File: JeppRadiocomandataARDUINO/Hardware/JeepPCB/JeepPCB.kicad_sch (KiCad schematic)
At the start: 10 parts

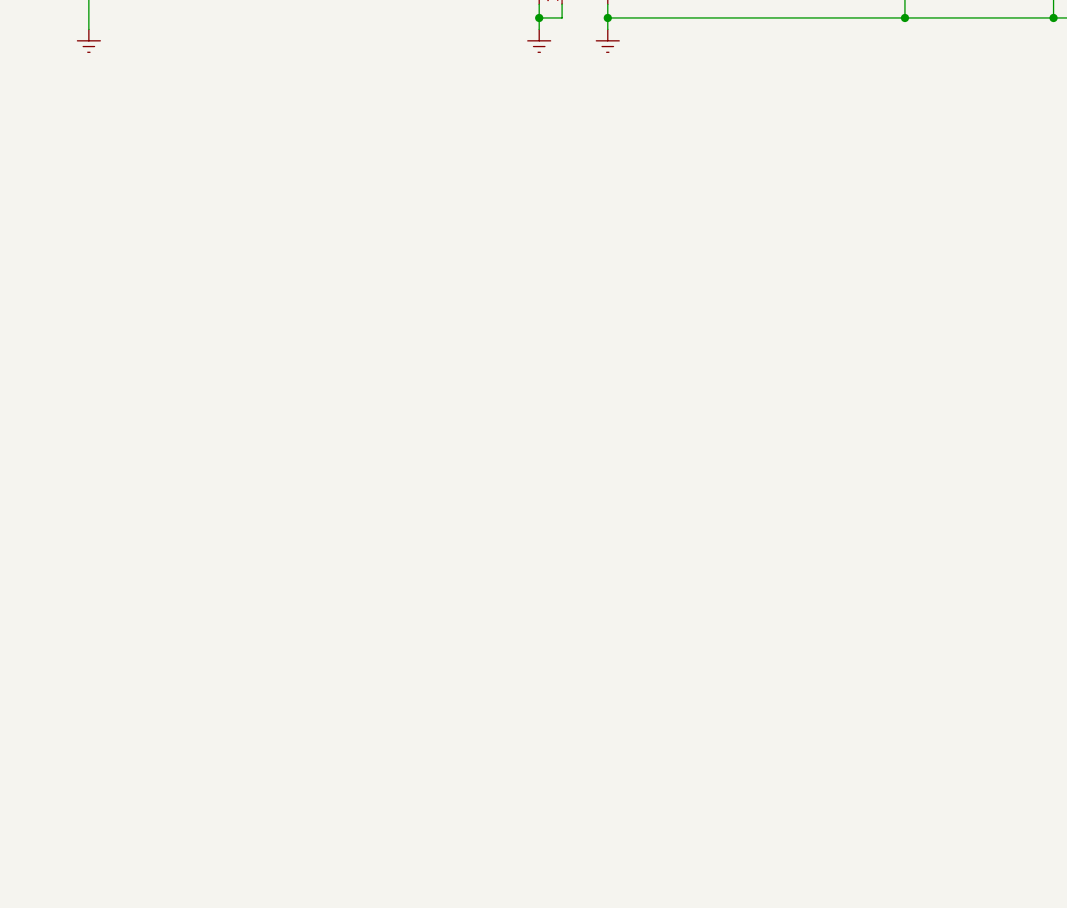
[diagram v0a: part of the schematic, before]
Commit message: Aggiunta della CPU ATmega328P
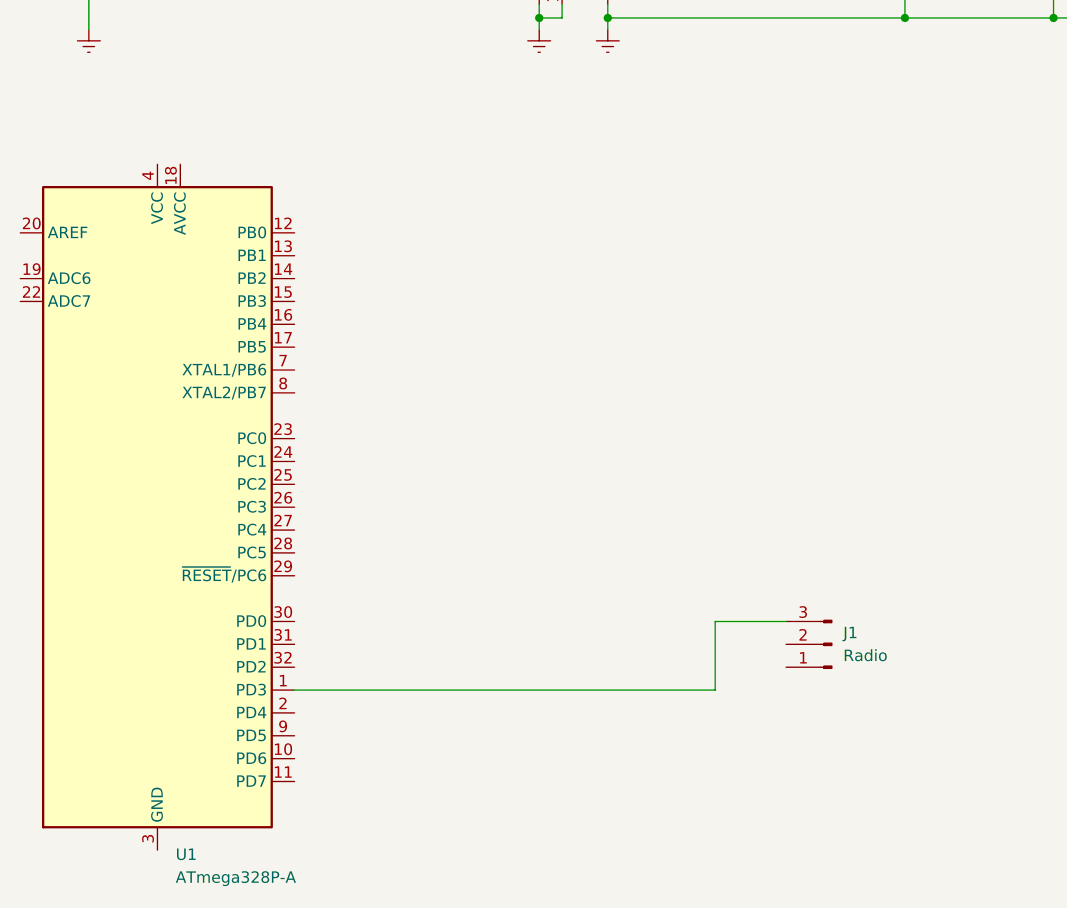
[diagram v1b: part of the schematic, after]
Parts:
- added J1: Radio, Connector_PinHeader_1.00mm:PinHeader_1x03_P1.00mm_Vertical, symbol Connector:Conn_01x03_Male
- added U1: ATmega328P-A, Package_QFP:TQFP-32_7x7mm_P0.8mm, symbol MCU_Microchip_ATmega:ATmega328P-A
- D1, D2, D3, D4, D5, D6, D7, D8: footprint Diode_THT:D_DO-41_SOD81_P10.16mm_Horizontal -> Diode_SMD:D_0402_1005Metric_Pad0.77x0.64mm_HandSolder
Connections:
- new net: J1.3 (Pin_3), U1.1 (PD3)
- new net: U1.21 (GND), U1.3 (GND), U1.5 (GND)
- new net: U1.4 (VCC), U1.6 (VCC)
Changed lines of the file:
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@@
   (junction (at 132.588 50.8) (diameter 0) (color 0 0 0 0)
   )
+  (junction (at 147.574 82.296) (diameter 0) (color 0 0 0 0)
+  )
+  (junction (at 147.574 53.848) (diameter 0) (color 0 0 0 0)
+  )
+  (junction (at 75.438 82.296) (diameter 0) (color 0 0 0 0)
+  )
+  (junction (at 116.078 57.912) (diameter 0) (color 0 0 0 0)
+  )
   (junction (at 83.058 82.296) (diameter 0) (color 0 0 0 0)
   )
-  (junction (at 147.574 82.296) (diameter 0) (color 0 0 0 0)
-  )
-  (junction (at 147.574 53.848) (diameter 0) (color 0 0 0 0)
-  )
-  (junction (at 75.438 82.296) (diameter 0) (color 0 0 0 0)
-  )
-  (junction (at 116.078 57.912) (diameter 0) (color 0 0 0 0)
-  )
   (junction (at 132.588 60.452) (diameter 0) (color 0 0 0 0)
   )
@@
     (stroke (width 0) (type default) (color 0 0 0 0))
   )
+  (wire (pts (xy 83.058 80.772) (xy 83.058 82.296))
+    (stroke (width 0) (type default) (color 0 0 0 0))
+  )
   (wire (pts (xy 98.298 65.532) (xy 147.574 65.532))
     (stroke (width 0) (type default) (color 0 0 0 0))
@@
     (stroke (width 0) (type default) (color 0 0 0 0))
   )
-  (wire (pts (xy 83.058 80.772) (xy 83.058 82.296))
+  (wire (pts (xy 48.26 156.972) (xy 94.996 156.972))
     (stroke (width 0) (type default) (color 0 0 0 0))
   )
@@
     (stroke (width 0) (type default) (color 0 0 0 0))
   )
+  (wire (pts (xy 94.996 149.352) (xy 102.87 149.352))
+    (stroke (width 0) (type default) (color 0 0 0 0))
+  )
   (wire (pts (xy 147.574 80.01) (xy 147.574 82.296))
     (stroke (width 0) (type default) (color 0 0 0 0))
@@
   )
   (wire (pts (xy 116.078 82.296) (xy 132.588 82.296))
+    (stroke (width 0) (type default) (color 0 0 0 0))
+  )
+  (wire (pts (xy 94.996 149.352) (xy 94.996 156.972))
     (stroke (width 0) (type default) (color 0 0 0 0))
   )
@@
       (effects (font (size 1.27 1.27)) (justify left))
     )
-    (property "Footprint" "Diode_THT:D_DO-41_SOD81_P10.16mm_Horizontal" (id 2) (at 111.633 38.608 0)
+    (property "Footprint" "Diode_SMD:D_0402_1005Metric_Pad0.77x0.64mm_HandSolder" (id 2) (at 111.633 38.608 0)
       (effects (font (size 1.27 1.27)) hide)
     )
@@
       (effects (font (size 1.27 1.27)) (justify left))
     )
-    (property "Footprint" "Diode_THT:D_DO-41_SOD81_P10.16mm_Horizontal" (id 2) (at 143.129 38.608 0)
+    (property "Footprint" "Diode_SMD:D_0402_1005Metric_Pad0.77x0.64mm_HandSolder" (id 2) (at 143.129 38.608 0)
       (effects (font (size 1.27 1.27)) hide)
     )
@@
       (effects (font (size 1.27 1.27)) (justify left))
     )
-    (property "Footprint" "Diode_THT:D_DO-41_SOD81_P10.16mm_Horizontal" (id 2) (at 160.655 76.2 0)
+    (property "Footprint" "Diode_SMD:D_0402_1005Metric_Pad0.77x0.64mm_HandSolder" (id 2) (at 160.655 76.2 0)
       (effects (font (size 1.27 1.27)) hide)
     )
@@
       (effects (font (size 1.27 1.27)) (justify left))
     )
-    (property "Footprint" "Diode_THT:D_DO-41_SOD81_P10.16mm_Horizontal" (id 2) (at 160.655 38.608 0)
+    (property "Footprint" "Diode_SMD:D_0402_1005Metric_Pad0.77x0.64mm_HandSolder" (id 2) (at 160.655 38.608 0)
       (effects (font (size 1.27 1.27)) hide)
     )
@@
       (effects (font (size 1.27 1.27)) (justify left))
     )
-    (property "Footprint" "Diode_THT:D_DO-41_SOD81_P10.16mm_Horizontal" (id 2) (at 111.633 76.2 0)
+    (property "Footprint" "Diode_SMD:D_0402_1005Metric_Pad0.77x0.64mm_HandSolder" (id 2) (at 111.633 76.2 0)
       (effects (font (size 1.27 1.27)) hide)
     )
@@
     (pin "2")
   )
+  (symbol (lib_id "Connector:Conn_01x03_Male") (at 107.95 151.892 180) (unit 1)
+    (in_bom yes) (on_board yes) (fields_autoplaced)
+    (property "Reference" "J1" (id 0) (at 109.22 150.6219 0)
+      (effects (font (size 1.27 1.27)) (justify right))
+    )
+    (property "Value" "Radio" (id 1) (at 109.22 153.1619 0)
+      (effects (font (size 1.27 1.27)) (justify right))
+    )
+    (property "Footprint" "Connector_PinHeader_1.00mm:PinHeader_1x03_P1.00mm_Vertical" (id 2) (at 107.95 151.892 0)
+      (effects (font (size 1.27 1.27)) hide)
+    )
+    (property "Datasheet" "~" (id 3) (at 107.95 151.892 0)
+      (effects (font (size 1.27 1.27)) hide)
+    )
+    (pin "1")
+    (pin "2")
+    (pin "3")
+  )
+  (symbol (lib_id "MCU_Microchip_ATmega:ATmega328P-A") (at 33.02 136.652 0) (unit 1)
+    (in_bom yes) (on_board yes) (fields_autoplaced)
+    (property "Reference" "U1" (id 0) (at 35.0394 175.26 0)
+      (effects (font (size 1.27 1.27)) (justify left))
+    )
+    (property "Value" "ATmega328P-A" (id 1) (at 35.0394 177.8 0)
+      (effects (font (size 1.27 1.27)) (justify left))
+    )
+    (property "Footprint" "Package_QFP:TQFP-32_7x7mm_P0.8mm" (id 2) (at 33.02 136.652 0)
+      (effects (font (size 1.27 1.27) italic) hide)
+    )
+    (property "Datasheet" "http://ww1.microchip.com/downloads/en/DeviceDoc/ATmega328_P%20AVR%20MCU%20with%20picoPower%20Technology%20Data%20Sheet%2040001984A.pdf" (id 3) (at 33.02 136.652 0)
+      (effects (font (size 1.27 1.27)) hide)
+    )
+    (pin "1")
+    (pin "10")
+    (pin "11")
+    (pin "12")
+    (pin "13")
+    (pin "14")
+    (pin "15")
+    (pin "16")
+    (pin "17")
+    (pin "18")
+    (pin "19")
+    (pin "2")
+    (pin "20")
+    (pin "21")
+    (pin "22")
+    (pin "23")
+    (pin "24")
+    (pin "25")
+    (pin "26")
+    (pin "27")
+    (pin "28")
+    (pin "29")
+    (pin "3")
+    (pin "30")
+    (pin "31")
+    (pin "32")
+    (pin "4")
+    (pin "5")
+    (pin "6")
+    (pin "7")
+    (pin "8")
+    (pin "9")
+  )
   (symbol (lib_id "Diode:1N4007") (at 147.574 76.2 270) (unit 1)
     (in_bom yes) (on_board yes) (fields_autoplaced)
@@
       (effects (font (size 1.27 1.27)) (justify left))
     )
-    (property "Footprint" "Diode_THT:D_DO-41_SOD81_P10.16mm_Horizontal" (id 2) (at 143.129 76.2 0)
+    (property "Footprint" "Diode_SMD:D_0402_1005Metric_Pad0.77x0.64mm_HandSolder" (id 2) (at 143.129 76.2 0)
       (effects (font (size 1.27 1.27)) hide)
     )
@@
       (effects (font (size 1.27 1.27)) (justify left))
     )
-    (property "Footprint" "Diode_THT:D_DO-41_SOD81_P10.16mm_Horizontal" (id 2) (at 128.143 38.608 0)
+    (property "Footprint" "Diode_SMD:D_0402_1005Metric_Pad0.77x0.64mm_HandSolder" (id 2) (at 128.143 38.608 0)
       (effects (font (size 1.27 1.27)) hide)
     )
@@
       (effects (font (size 1.27 1.27)) (justify left))
     )
-    (property "Footprint" "Diode_THT:D_DO-41_SOD81_P10.16mm_Horizontal" (id 2) (at 128.143 76.2 0)
+    (property "Footprint" "Diode_SMD:D_0402_1005Metric_Pad0.77x0.64mm_HandSolder" (id 2) (at 128.143 76.2 0)
       (effects (font (size 1.27 1.27)) hide)
     )
@@
     )
     (path "/bca904a5-95f1-4635-a3fd-e82f967da29e"
-      (reference "D1") (unit 1) (value "1N4007") (footprint "Diode_THT:D_DO-41_SOD81_P10.16mm_Horizontal")
+      (reference "D1") (unit 1) (value "1N4007") (footprint "Diode_SMD:D_0402_1005Metric_Pad0.77x0.64mm_HandSolder")
     )
     (path "/f1b2559a-d03d-485e-9014-6d5a85429488"
-      (reference "D2") (unit 1) (value "1N4007") (footprint "Diode_THT:D_DO-41_SOD81_P10.16mm_Horizontal")
+      (reference "D2") (unit 1) (value "1N4007") (footprint "Diode_SMD:D_0402_1005Metric_Pad0.77x0.64mm_HandSolder")
     )
     (path "/d15003af-1ed1-4452-98ac-086219aa30ea"
-      (reference "D3") (unit 1) (value "1N4007") (footprint "Diode_THT:D_DO-41_SOD81_P10.16mm_Horizontal")
+      (reference "D3") (unit 1) (value "1N4007") (footprint "Diode_SMD:D_0402_1005Metric_Pad0.77x0.64mm_HandSolder")
     )
     (path "/7e464a84-08f9-4f2c-88d3-1e115916ba1b"
-      (reference "D4") (unit 1) (value "1N4007") (footprint "Diode_THT:D_DO-41_SOD81_P10.16mm_Horizontal")
+      (reference "D4") (unit 1) (value "1N4007") (footprint "Diode_SMD:D_0402_1005Metric_Pad0.77x0.64mm_HandSolder")
     )
     (path "/0a3d4bf5-488d-4f46-a8d6-8e678e8fff8c"
-      (reference "D5") (unit 1) (value "1N4007") (footprint "Diode_THT:D_DO-41_SOD81_P10.16mm_Horizontal")
+      (reference "D5") (unit 1) (value "1N4007") (footprint "Diode_SMD:D_0402_1005Metric_Pad0.77x0.64mm_HandSolder")
     )
     (path "/e5594bd3-4d0f-483e-9068-0f7050e764c1"
-      (reference "D6") (unit 1) (value "1N4007") (footprint "Diode_THT:D_DO-41_SOD81_P10.16mm_Horizontal")
+      (reference "D6") (unit 1) (value "1N4007") (footprint "Diode_SMD:D_0402_1005Metric_Pad0.77x0.64mm_HandSolder")
     )
     (path "/19adf11e-7325-4e78-9ced-a208432b681c"
-      (reference "D7") (unit 1) (value "1N4007") (footprint "Diode_THT:D_DO-41_SOD81_P10.16mm_Horizontal")
+      (reference "D7") (unit 1) (value "1N4007") (footprint "Diode_SMD:D_0402_1005Metric_Pad0.77x0.64mm_HandSolder")
     )
     (path "/8cab1a5e-20a8-4b1b-ae9e-f9d96b7e6a4d"
-      (reference "D8") (unit 1) (value "1N4007") (footprint "Diode_THT:D_DO-41_SOD81_P10.16mm_Horizontal")
+      (reference "D8") (unit 1) (value "1N4007") (footprint "Diode_SMD:D_0402_1005Metric_Pad0.77x0.64mm_HandSolder")
+    )
+    (path "/c6ff950c-fe73-4725-a0da-2103c5405644"
+      (reference "J1") (unit 1) (value "Radio") (footprint "Connector_PinHeader_1.00mm:PinHeader_1x03_P1.00mm_Vertical")
     )
     (path "/683e3a53-02e9-4f1e-85e1-798d9013c0f4"
       (reference "MotorFET1") (unit 1) (value "L298N") (footprint "Package_TO_SOT_THT:TO-220-15_P2.54x2.54mm_StaggerOdd_Lead4.58mm_Vertical")
     )
-  )
+    (path "/c751029c-0ca6-4cd0-8725-946b9af36995"
+      (reference "U1") (unit 1) (value "ATmega328P-A") (footprint "Package_QFP:TQFP-32_7x7mm_P0.8mm")
+    )
+  )

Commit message: Aggiornamento del PCB
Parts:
- added REG_LIN1: KA78M05_TO252, Package_TO_SOT_SMD:TO-252-2, symbol Regulator_Linear:KA78M05_TO252
- added C2: 220uF, Capacitor_SMD:C_Elec_4x5.8, symbol Device:C_Polarized_US
- added J_BACK1, J_FRONT1: Screw_Terminal_01x02, TerminalBlock_Phoenix:TerminalBlock_Phoenix_MKDS-1,5-2-5.08_1x02_P5.08mm_Horizontal, symbol Connector:Screw_Terminal_01x02
- added J_MAIN_POWER1: Screw_Terminal_01x03, TerminalBlock_Phoenix:TerminalBlock_Phoenix_MKDS-1,5-3_1x03_P5.00mm_Horizontal, symbol Connector:Screw_Terminal_01x03
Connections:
- net Earth: now also J1.1 (Pin_1), U1.21 (GND), U1.3 (GND), U1.5 (GND), REG_LIN1.2 (GND), C2.2, J_MAIN_POWER1.2 (Pin_2)
- net at C1.1, D5.1 (K), D6.1 (K)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: now also REG_LIN1.1 (VI), J_MAIN_POWER1.1 (Pin_1)
- net INO_D7: now reaches MotorFET1.10 (IN3)
- net INO_D5: now reaches MotorFET1.11 (EnB)
- net INO_D6: now reaches MotorFET1.12 (IN4)
- net INO_D9: now reaches MotorFET1.5 (IN1)
- net INO_D10: now reaches MotorFET1.6 (EnA)
- net INO_D8: now reaches MotorFET1.7 (IN2)
- net at MotorFET1.9 (Vss): now also REG_LIN1.3 (VO), C2.1, J_MAIN_POWER1.3 (Pin_3)
- net OUT1: no longer names the net of D1.1 (K), D5.2 (A), MotorFET1.2 (OUT1)
- net OUT1: now also J_FRONT1.1 (Pin_1)
- net OUT2: no longer names the net of D2.1 (K), D6.2 (A), MotorFET1.3 (OUT2)
- net OUT2: now also J_FRONT1.2 (Pin_2)
- net OUT3: no longer names the net of D3.1 (K), D7.2 (A), MotorFET1.13 (OUT3)
- net OUT3: now also J_BACK1.1 (Pin_1)
- net OUT4: no longer names the net of D4.1 (K), D8.2 (A), MotorFET1.14 (OUT4)
- net OUT4: now also J_BACK1.2 (Pin_2)
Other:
- title: (none) -> Jepp Radiocomandata
- moved on the sheet: J1, U1
